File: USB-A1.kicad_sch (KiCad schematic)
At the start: 24 parts, among them J10 USB3_A, J9 USB3_A, U16 UCS2114-1-V/G4, U17 TPD4E02B04DQA, U18 TPD4E02B04DQA

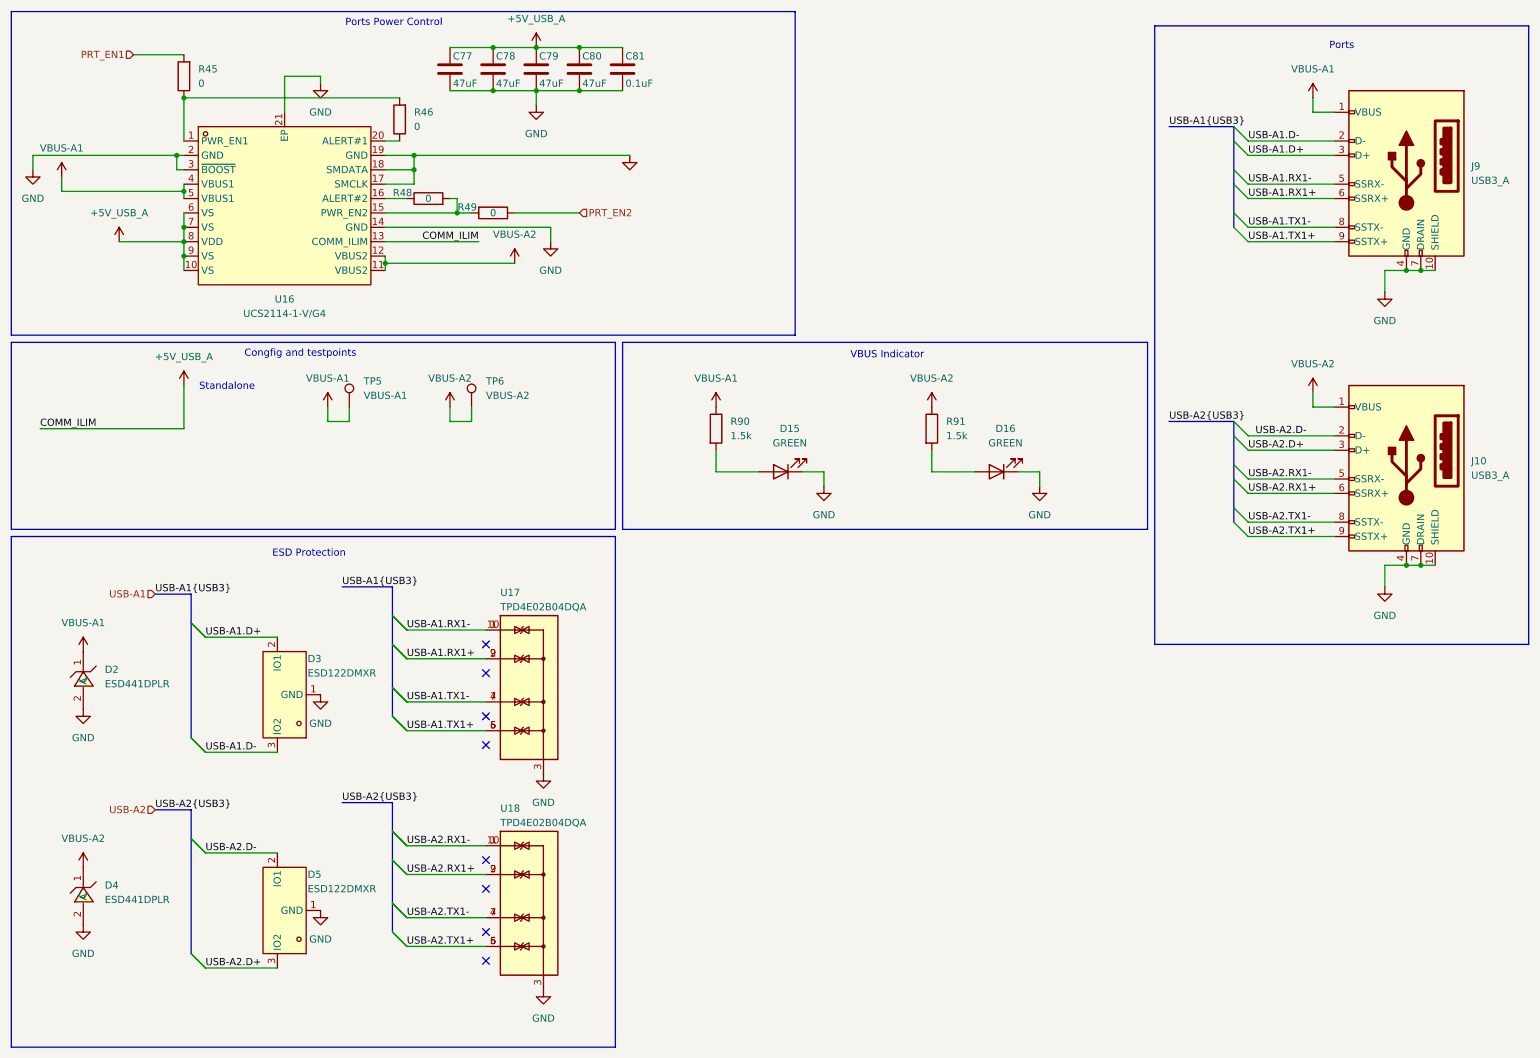
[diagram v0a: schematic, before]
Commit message: Schematic reannotated
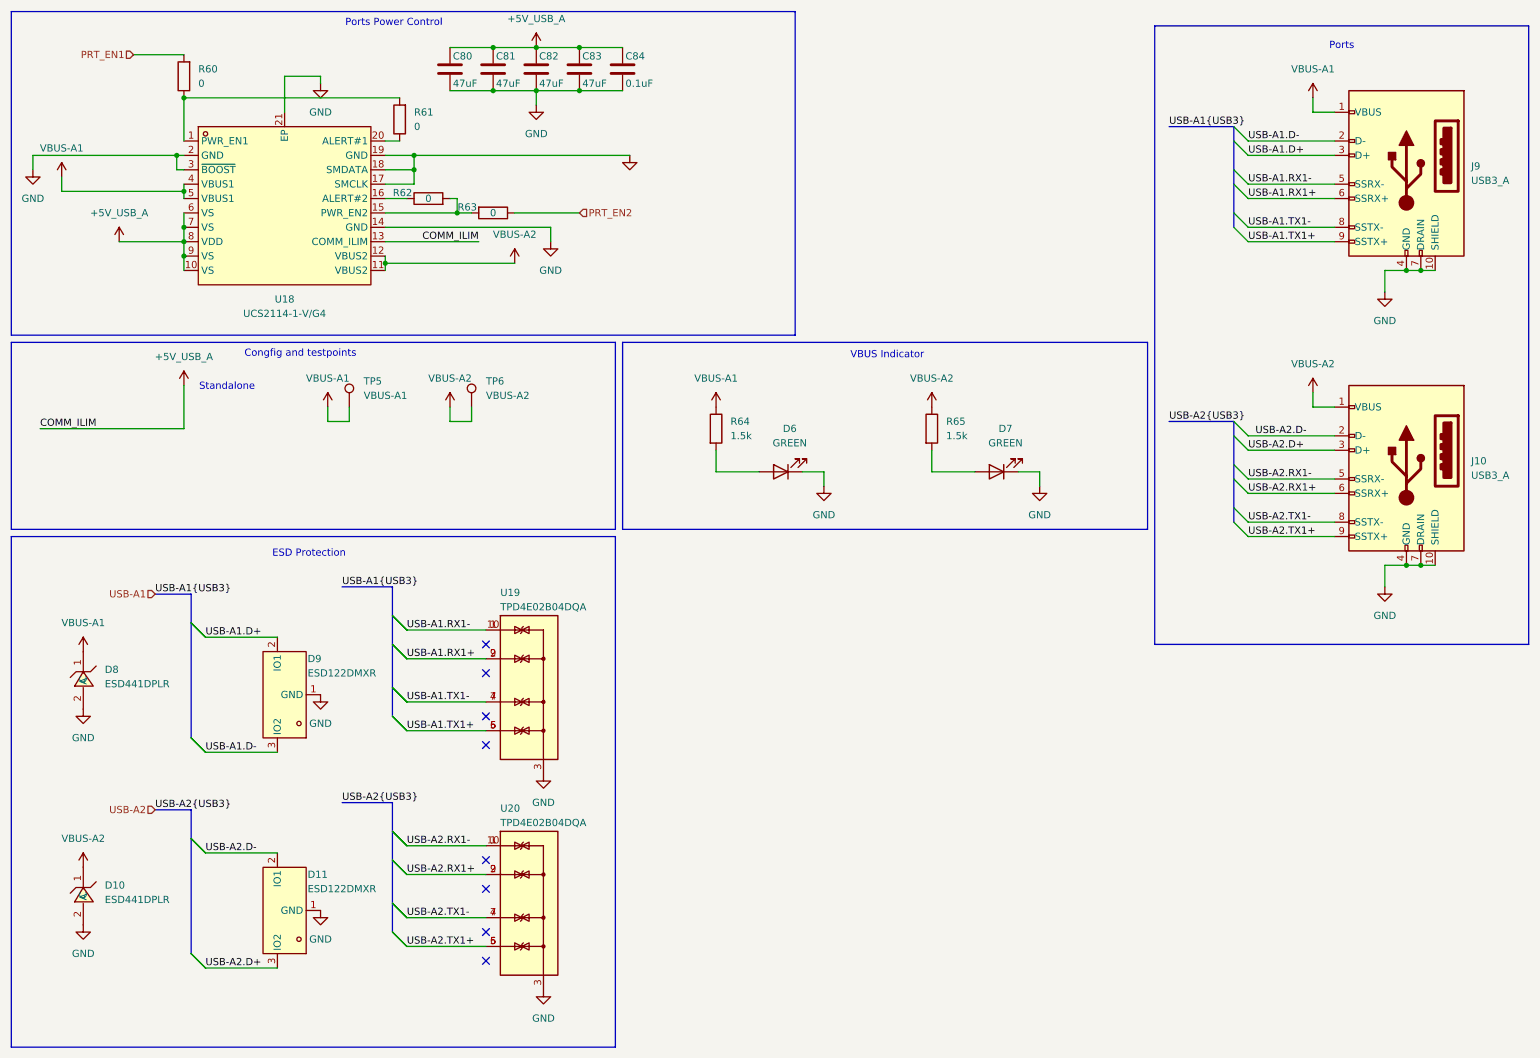
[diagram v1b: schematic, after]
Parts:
- renumbered C77 to C80, C78 to C81, C79 to C82, C80 to C83, C81 to C84, D4 to D10, D5 to D11, D15 to D6, D16 to D7, D2 to D8, D3 to D9, R45 to R60, R46 to R61, R48 to R62, R49 to R63, R90 to R64, R91 to R65, U16 to U18, U17 to U19, U18 to U20

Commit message: J11 changed to 8-pin PCIe connector, footprint assigned
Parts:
- D6, D7: footprint (none) -> LED_SMD:LED_0603_1608Metric
- J10, J9: footprint Connector_USB:USB3_A_Molex_48393-001 -> SamacSys_Parts:GSB4116344HR
- R64, R65: footprint (none) -> Resistor_SMD:R_0402_1005Metric
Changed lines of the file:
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@@
 			)
 		)
-		(property "Footprint" ""
+		(property "Footprint" "Resistor_SMD:R_0402_1005Metric"
 			(at 176.022 86.36 90)
 			(effects
@@
 			)
 		)
-		(property "Footprint" ""
+		(property "Footprint" "LED_SMD:LED_0603_1608Metric"
 			(at 189.23 93.98 0)
 			(effects
@@
 			)
 		)
-		(property "Footprint" "Connector_USB:USB3_A_Molex_48393-001"
+		(property "Footprint" "SamacSys_Parts:GSB4116344HR"
 			(at 257.81 38.1 0)
 			(effects
@@
 			)
 		)
-		(property "Footprint" ""
+		(property "Footprint" "LED_SMD:LED_0603_1608Metric"
 			(at 151.13 93.98 0)
 			(effects
@@
 			)
 		)
-		(property "Footprint" "Connector_USB:USB3_A_Molex_48393-001"
+		(property "Footprint" "SamacSys_Parts:GSB4116344HR"
 			(at 257.81 90.17 0)
 			(effects
@@
 			)
 		)
-		(property "Footprint" ""
+		(property "Footprint" "Resistor_SMD:R_0402_1005Metric"
 			(at 137.922 86.36 90)
 			(effects

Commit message: footprints assigned, U21 change to SiRA80DP
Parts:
- TP5, TP6: footprint TestPoint:TestPoint_THTPad_1.5x1.5mm_Drill0.7mm -> TestPoint:TestPoint_Loop_D1.80mm_Drill1.0mm_Beaded
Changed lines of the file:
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@@
 			)
 		)
-		(property "Footprint" "TestPoint:TestPoint_THTPad_1.5x1.5mm_Drill0.7mm"
+		(property "Footprint" "TestPoint:TestPoint_Loop_D1.80mm_Drill1.0mm_Beaded"
 			(at 101.6 82.55 0)
 			(effects
@@
 			)
 		)
-		(property "Footprint" "TestPoint:TestPoint_THTPad_1.5x1.5mm_Drill0.7mm"
+		(property "Footprint" "TestPoint:TestPoint_Loop_D1.80mm_Drill1.0mm_Beaded"
 			(at 80.01 82.55 0)
 			(effects

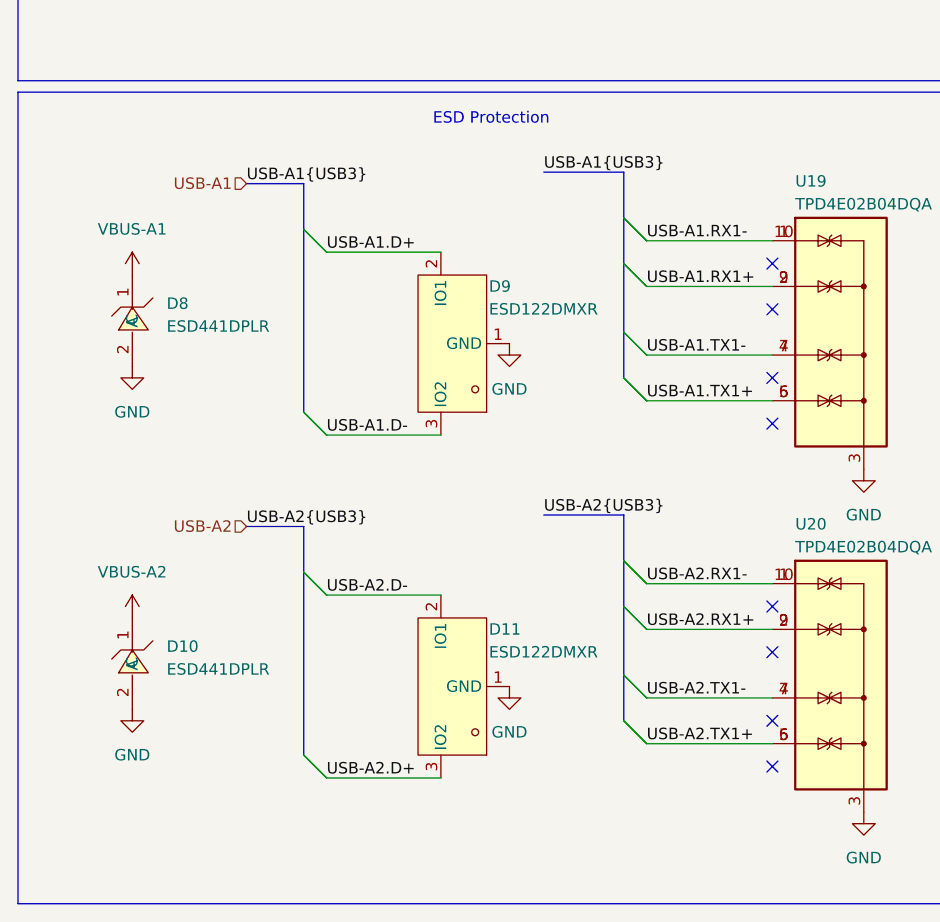
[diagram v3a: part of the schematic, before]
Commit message: Next net class label fixes, swap of the SS lines for better routing
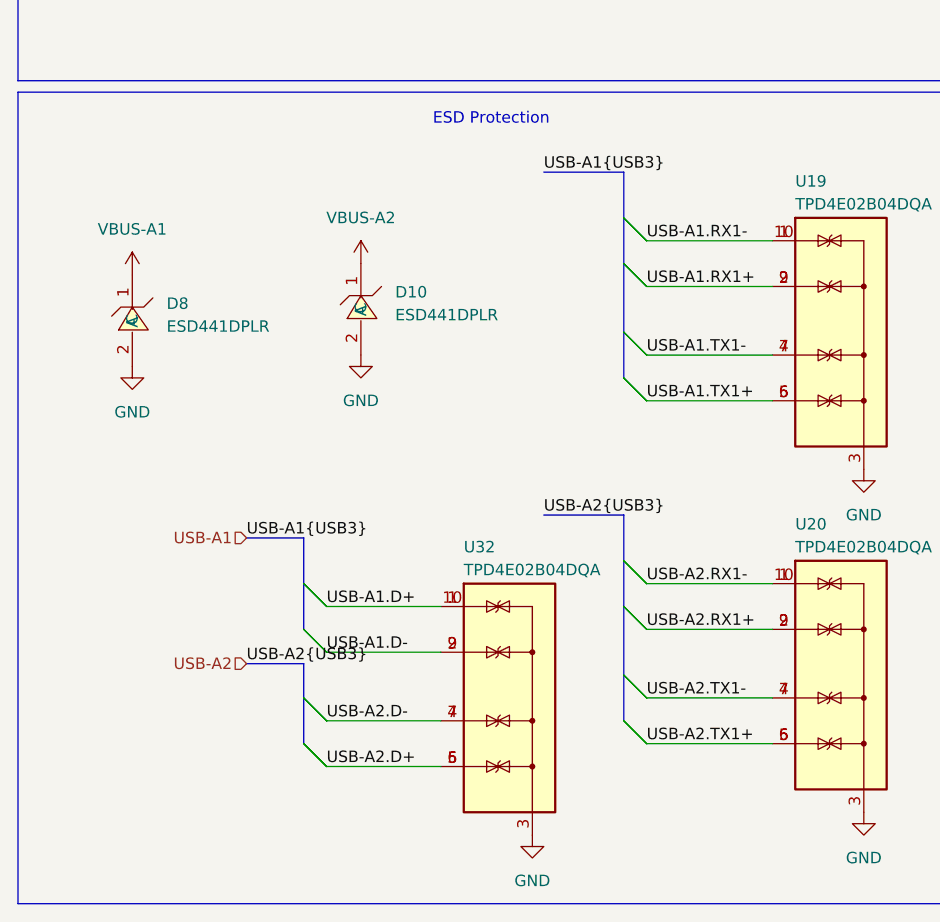
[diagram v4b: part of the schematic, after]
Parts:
- removed D11, D9: ESD122DMXR, EasyEDA:X2SON-3_L1.0-W0.6-L, symbol EasyEDA:ESD122DMXR
- added U32: TPD4E02B04DQA, Package_SON:USON-10_2.5x1.0mm_P0.5mm, symbol Snapeda:TPD4E02B04DQA
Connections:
- net GND: now also U32.3 (G), U32.8 (G)
- net USB-A1.D+: now also U32.1 (IO1), U32.10 (NC)
- net USB-A1.D-: now also U32.2 (IO2), U32.9 (NC)
- net USB-A2.D+: now also U32.5 (IO4), U32.6 (NC)
- net USB-A2.D-: now also U32.4 (IO3), U32.7 (NC)
- no-connect marks 8 -> 0
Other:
- moved on the sheet: D10

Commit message: Added lcsc part number for most of components, fixes for better routing
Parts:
- C80, C81, C82, C83: footprint Capacitor_THT:C_Radial_D10.0mm_H16.0mm_P5.00mm -> Capacitor_THT:C_Radial_D5.0mm_H11.0mm_P2.00mm; LCSC Part (none) -> C721300
- C84: LCSC Part (none) -> C5182432
- D6, D7: LCSC Part (none) -> C22371298
- U19, U20, U32: LCSC Part (none) -> C106794
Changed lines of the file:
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@@
+			)
+		)
+		(property "LCSC Part" "C106794"
+			(at 106.68 170.18 0)
+			(effects
+				(font
+					(size 1.27 1.27)
+				)
+				(hide yes)
 			)
 		)
@@
 			)
 		)
+		(property "LCSC Part" "C106794"
+			(at 69.85 172.72 0)
+			(effects
+				(font
+					(size 1.27 1.27)
+				)
+				(hide yes)
+			)
+		)
 		(pin "5"
 		)
@@
 		)
 		(property "Sim.Pins" "1=K 2=A"
+			(at 189.23 93.98 0)
+			(effects
+				(font
+					(size 1.27 1.27)
+				)
+				(hide yes)
+			)
+		)
+		(property "LCSC Part" "C22371298"
 			(at 189.23 93.98 0)
 			(effects
@@
 			)
 		)
-		(property "Footprint" "Capacitor_THT:C_Radial_D10.0mm_H16.0mm_P5.00mm"
+		(property "Footprint" "Capacitor_THT:C_Radial_D5.0mm_H11.0mm_P2.00mm"
 			(at 108.9152 26.67 0)
 			(effects
@@
 		)
 		(property "Description" "Unpolarized capacitor"
+			(at 107.95 22.86 0)
+			(effects
+				(font
+					(size 1.27 1.27)
+				)
+				(hide yes)
+			)
+		)
+		(property "LCSC Part" "C721300"
 			(at 107.95 22.86 0)
 			(effects
@@
 			)
 		)
+		(property "LCSC Part" "C5182432"
+			(at 123.19 22.86 0)
+			(effects
+				(font
+					(size 1.27 1.27)
+				)
+				(hide yes)
+			)
+		)
 		(pin "1"
 		)
@@
 			)
 		)
-		(property "Footprint" "Capacitor_THT:C_Radial_D10.0mm_H16.0mm_P5.00mm"
+		(property "Footprint" "Capacitor_THT:C_Radial_D5.0mm_H11.0mm_P2.00mm"
 			(at 116.5352 26.67 0)
 			(effects
@@
 			)
 		)
+		(property "LCSC Part" "C721300"
+			(at 115.57 22.86 0)
+			(effects
+				(font
+					(size 1.27 1.27)
+				)
+				(hide yes)
+			)
+		)
 		(pin "1"
 		)
@@
 			)
 		)
-		(property "Footprint" "Capacitor_THT:C_Radial_D10.0mm_H16.0mm_P5.00mm"
+		(property "Footprint" "Capacitor_THT:C_Radial_D5.0mm_H11.0mm_P2.00mm"
 			(at 93.6752 26.67 0)
 			(effects
@@
 			)
 		)
+		(property "LCSC Part" "C721300"
+			(at 92.71 22.86 0)
+			(effects
+				(font
+					(size 1.27 1.27)
+				)
+				(hide yes)
+			)
+		)
 		(pin "1"
 		)
@@
 			)
 		)
+		(property "LCSC Part" "C22371298"
+			(at 151.13 93.98 0)
+			(effects
+				(font
+					(size 1.27 1.27)
+				)
+				(hide yes)
+			)
+		)
 		(pin "1"
 		)
@@
 			)
 		)
-		(property "Footprint" "Capacitor_THT:C_Radial_D10.0mm_H16.0mm_P5.00mm"
+		(property "Footprint" "Capacitor_THT:C_Radial_D5.0mm_H11.0mm_P2.00mm"
 			(at 101.2952 26.67 0)
 			(effects
@@
 		)
 		(property "Description" "Unpolarized capacitor"
+			(at 100.33 22.86 0)
+			(effects
+				(font
+					(size 1.27 1.27)
+				)
+				(hide yes)
+			)
+		)
+		(property "LCSC Part" "C721300"
 			(at 100.33 22.86 0)
 			(effects
@@
 			(at 106.68 132.08 0)
 			(effects
+				(font
+					(size 1.27 1.27)
+				)
+				(hide yes)
+			)
+		)
+		(property "LCSC Part" "C106794"
+			(at 106.68 132.08 0)
+			(effects

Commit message: Added lcsc part number for most of resistors
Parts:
- J10, J9: LCSC Part (none) -> C5119948
- R60, R61, R62, R63: footprint Resistor_SMD:R_0402_1005Metric -> Resistor_SMD:R_0603_1608Metric; LCSC Part (none) -> C2906974
- R64, R65: LCSC Part (none) -> C327253
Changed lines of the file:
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@@
+			)
+		)
+		(property "LCSC Part" "C327253 "
+			(at 177.8 86.36 0)
+			(effects
+				(font
+					(size 1.27 1.27)
+				)
+				(hide yes)
 			)
 		)
@@
 			)
 		)
+		(property "LCSC Part" "C5119948 "
+			(at 261.62 40.64 0)
+			(effects
+				(font
+					(size 1.27 1.27)
+				)
+				(hide yes)
+			)
+		)
 		(pin "3"
 		)
@@
 			)
 		)
-		(property "Footprint" "Resistor_SMD:R_0402_1005Metric"
+		(property "Footprint" "Resistor_SMD:R_0603_1608Metric"
 			(at 47.498 24.13 90)
 			(effects
@@
 			)
 		)
+		(property "LCSC Part" "C2906974"
+			(at 45.72 24.13 0)
+			(effects
+				(font
+					(size 1.27 1.27)
+				)
+				(hide yes)
+			)
+		)
 		(pin "2"
 		)
@@
 			)
 		)
-		(property "Footprint" "Resistor_SMD:R_0402_1005Metric"
+		(property "Footprint" "Resistor_SMD:R_0603_1608Metric"
 			(at 100.33 46.482 90)
 			(effects
@@
 			)
 		)
+		(property "LCSC Part" "C2906974"
+			(at 100.33 48.26 90)
+			(effects
+				(font
+					(size 1.27 1.27)
+				)
+				(hide yes)
+			)
+		)
 		(pin "2"
 		)
@@
 			)
 		)
-		(property "Footprint" "Resistor_SMD:R_0402_1005Metric"
+		(property "Footprint" "Resistor_SMD:R_0603_1608Metric"
 			(at 88.9 47.498 90)
 			(effects
@@
 		(property "Description" "Resistor"
 			(at 88.9 45.72 0)
+			(effects
+				(font
+					(size 1.27 1.27)
+				)
+				(hide yes)
+			)
+		)
+		(property "LCSC Part" "C2906974"
+			(at 88.9 45.72 90)
 			(effects
 				(font
@@
 			)
 		)
+		(property "LCSC Part" "C5119948 "
+			(at 261.62 92.71 0)
+			(effects
+				(font
+					(size 1.27 1.27)
+				)
+				(hide yes)
+			)
+		)
 		(pin "3"
 		)
@@
 			)
 		)
+		(property "LCSC Part" "C327253 "
+			(at 139.7 86.36 0)
+			(effects
+				(font
+					(size 1.27 1.27)
+				)
+				(hide yes)
+			)
+		)
 		(pin "2"
 		)
@@
 			)
 		)
-		(property "Footprint" "Resistor_SMD:R_0402_1005Metric"
+		(property "Footprint" "Resistor_SMD:R_0603_1608Metric"
 			(at 85.598 31.75 90)
 			(effects
@@
 			(at 83.82 31.75 0)
 			(effects
+				(font
+					(size 1.27 1.27)
+				)
+				(hide yes)
+			)
+		)
+		(property "LCSC Part" "C2906974"
+			(at 83.82 31.75 0)
+			(effects
